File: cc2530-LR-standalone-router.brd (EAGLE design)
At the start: 44 x 24 mm, 16 parts, among them J1 629105150921, U1 AP2112K

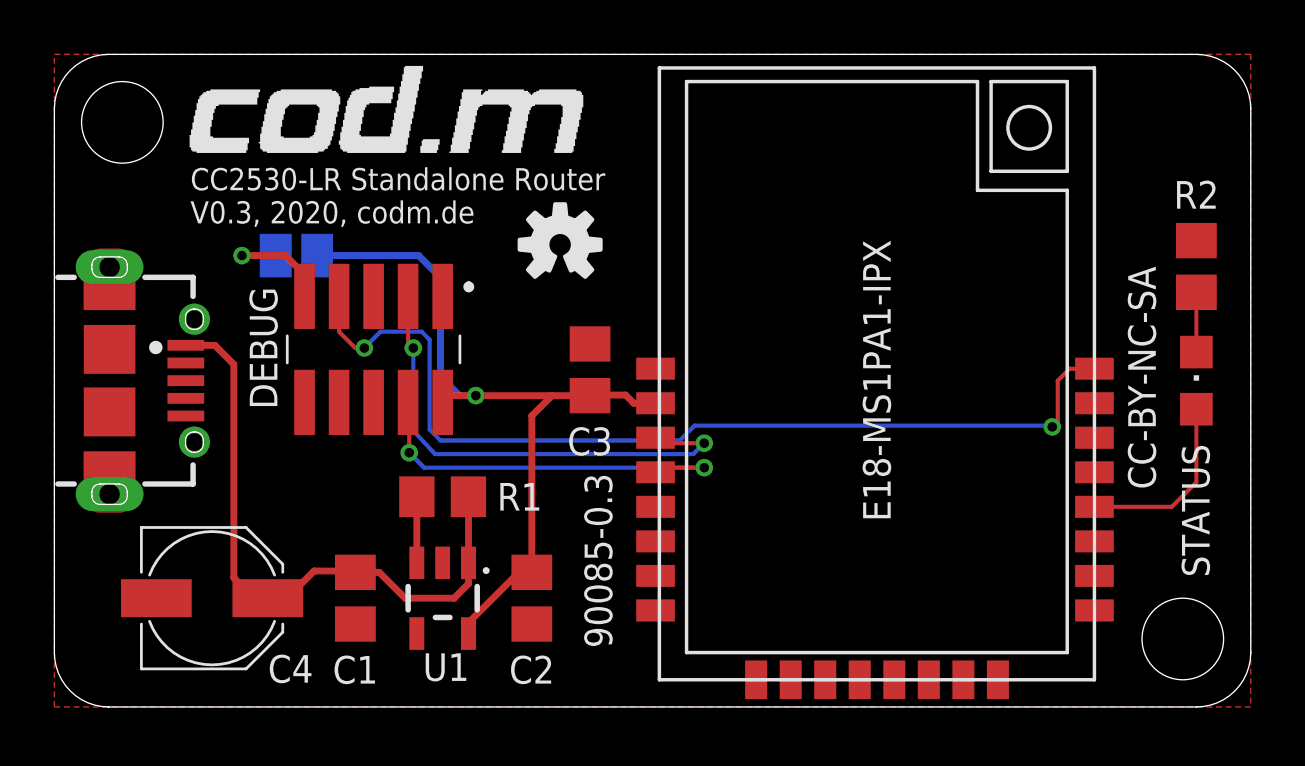
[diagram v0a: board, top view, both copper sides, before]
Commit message: minor rerouting
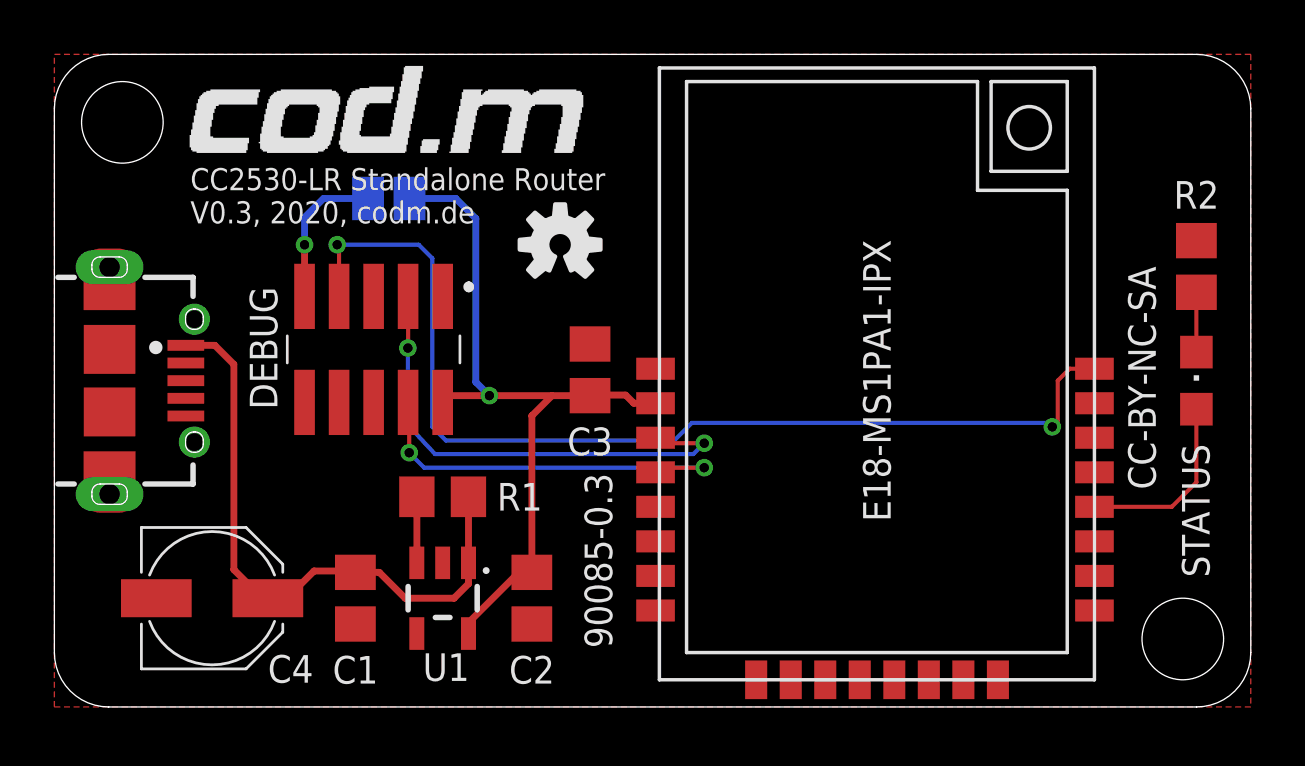
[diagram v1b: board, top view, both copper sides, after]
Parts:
- moved DBGVCC 4.00 mm to (12.3, 18.7)
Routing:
- net RST: track 35.2 -> 38.5 mm
- net VCC-DEBUG: track 4.63 -> 5.53 mm
- net VCC: track 28.5 -> 27.8 mm
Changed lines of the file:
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@@
 <attribute name="WORKING-VOLTAGE" value="30V(AC)" x="2.5" y="12" size="1.778" layer="27" rot="R270" display="off"/>
 </element>
-<element name="DBGVCC" library="jumper" library_urn="urn:adsk.eagle:library:252" package="SJ" package3d_urn="urn:adsk.eagle:package:15471/1" value="" x="8.9" y="16.6" smashed="yes" rot="MR0">
-<attribute name="NAME" x="12.151" y="17.843" size="1.27" layer="26" ratio="10" rot="MR0"/>
-<attribute name="POPULARITY" value="33" x="8.9" y="16.6" size="1.778" layer="28" rot="MR0" display="off"/>
-<attribute name="VALUE" x="8.4999" y="16.6" size="0.02" layer="28" rot="MR0"/>
+<element name="DBGVCC" library="jumper" library_urn="urn:adsk.eagle:library:252" package="SJ" package3d_urn="urn:adsk.eagle:package:15471/1" value="" x="12.3" y="18.7" smashed="yes" rot="MR0">
+<attribute name="NAME" x="15.551" y="19.943" size="1.27" layer="26" ratio="10" rot="MR0"/>
+<attribute name="POPULARITY" value="33" x="12.3" y="18.7" size="1.778" layer="28" rot="MR0" display="off"/>
+<attribute name="VALUE" x="11.8999" y="18.7" size="0.02" layer="28" rot="MR0"/>
 </element>
 <element name="U$2" library="codm" library_urn="urn:adsk.eagle:library:11602856" package="CODM-LOGO" package3d_urn="urn:adsk.eagle:package:11602917/4" value="" x="5" y="20.4" smashed="yes"/>
@@
 <wire x1="11.95" y1="4.95" x2="11.07" y2="4.95" width="0.254" layer="1"/>
 <wire x1="12.9" y1="4" x2="11.95" y2="4.95" width="0.254" layer="1"/>
-<wire x1="6.6" y1="12.6" x2="6.6" y2="4.75" width="0.254" layer="1"/>
-<wire x1="7.35" y1="4" x2="6.6" y2="4.75" width="0.254" layer="1"/>
+<wire x1="6.6" y1="12.6" x2="6.6" y2="5.05" width="0.254" layer="1"/>
 <wire x1="11.07" y1="4.95" x2="11.02" y2="5" width="0.254" layer="1"/>
 <wire x1="11.02" y1="5" x2="9.55" y2="5" width="0.254" layer="1"/>
@@
 <contactref element="C4" pad="+"/>
 <wire x1="7.85" y1="4" x2="8.55" y2="4" width="0.1524" layer="1"/>
-<wire x1="7.35" y1="4" x2="7.85" y2="4" width="0" layer="19" extent="1-1"/>
+<wire x1="6.6" y1="5.05" x2="7.65" y2="4" width="0.254" layer="1"/>
+<wire x1="7.65" y1="4" x2="7.85" y2="4" width="0.254" layer="1"/>
 </signal>
 <signal name="N$1">
@@
 <wire x1="17.0801" y1="4.95" x2="15.23" y2="3.0999" width="0.254" layer="1"/>
 <wire x1="17.0801" y1="4.95" x2="17.56" y2="4.95" width="0.254" layer="1"/>
-<wire x1="14.53" y1="11.45" x2="15.5" y2="11.45" width="0.254" layer="1"/>
+<wire x1="14.53" y1="11.45" x2="16" y2="11.45" width="0.254" layer="1"/>
 <wire x1="14.28" y1="11.2" x2="14.53" y2="11.45" width="0.254" layer="1"/>
 <wire x1="17.56" y1="4.95" x2="17.56" y2="10.71" width="0.254" layer="1"/>
 <contactref element="DBGVCC" pad="1"/>
-<wire x1="9.662" y1="16.6" x2="13.4" y2="16.6" width="0.254" layer="16"/>
-<wire x1="13.4" y1="16.6" x2="14.2" y2="15.8" width="0.254" layer="16"/>
-<wire x1="15.5" y1="11.45" x2="14.9" y2="11.45" width="0.254" layer="16"/>
-<wire x1="14.9" y1="11.45" x2="14.2" y2="12.15" width="0.254" layer="16"/>
-<wire x1="14.2" y1="15.8" x2="14.2" y2="12.15" width="0.254" layer="16"/>
-<via x="15.5" y="11.45" extent="1-16" drill="0.35" shape="octagon"/>
+<wire x1="14.762" y1="18.7" x2="15.5" y2="17.962" width="0.254" layer="16"/>
+<wire x1="14.762" y1="18.7" x2="13.062" y2="18.7" width="0.254" layer="16"/>
 <wire x1="19.7" y1="11.45" x2="19.72" y2="11.47" width="0.254" layer="1"/>
-<wire x1="22.11" y1="11.17" x2="22" y2="11.17" width="0.254" layer="1"/>
-<wire x1="22" y1="11.17" x2="21.31" y2="11.17" width="0.254" layer="1"/>
+<wire x1="22.11" y1="11.17" x2="21.31" y2="11.17" width="0.254" layer="1"/>
 <wire x1="21.31" y1="11.17" x2="21.01" y2="11.47" width="0.254" layer="1"/>
 <wire x1="21.01" y1="11.47" x2="19.72" y2="11.47" width="0.254" layer="1"/>
 <wire x1="17.56" y1="10.71" x2="18.3" y2="11.45" width="0.254" layer="1"/>
 <wire x1="18.3" y1="11.45" x2="19.7" y2="11.45" width="0.254" layer="1"/>
-<wire x1="15.5" y1="11.45" x2="18.3" y2="11.45" width="0.254" layer="1"/>
+<wire x1="16" y1="11.45" x2="18.3" y2="11.45" width="0.254" layer="1"/>
+<wire x1="15.5" y1="11.95" x2="16" y2="11.45" width="0.254" layer="16"/>
+<via x="16" y="11.45" extent="1-16" drill="0.35" shape="octagon"/>
+<wire x1="15.5" y1="17.962" x2="15.5" y2="11.95" width="0.254" layer="16"/>
 </signal>
 <signal name="DD">
@@
 <contactref element="U$5" pad="P2.2"/>
 <contactref element="DEBUG" pad="3"/>
-<wire x1="13.01" y1="15.1" x2="13.01" y2="13.39" width="0.1524" layer="1"/>
-<wire x1="13.01" y1="13.39" x2="13.2" y2="13.2" width="0.1524" layer="1"/>
-<via x="13.2" y="13.2" extent="1-16" drill="0.35" shape="octagon"/>
-<wire x1="13.2" y1="13.2" x2="13.2" y2="10.159884375" width="0.1524" layer="16"/>
-<wire x1="13.2" y1="10.159884375" x2="14" y2="9.3" width="0.1524" layer="16"/>
+<wire x1="13.01" y1="15.1" x2="13.01" y2="13.21" width="0.1524" layer="1"/>
+<wire x1="13.01" y1="13.21" x2="13" y2="13.2" width="0.1524" layer="1"/>
+<via x="13" y="13.2" extent="1-16" drill="0.35" shape="octagon"/>
+<wire x1="13" y1="13.2" x2="13" y2="10.37485625" width="0.1524" layer="16"/>
+<wire x1="13" y1="10.37485625" x2="14" y2="9.3" width="0.1524" layer="16"/>
 <wire x1="23.5" y1="9.3" x2="14" y2="9.3" width="0.1524" layer="16"/>
 <wire x1="23.5" y1="9.3" x2="23.9" y2="9.7" width="0.1524" layer="16"/>
@@
 <wire x1="36.9" y1="10.5" x2="36.7" y2="10.3" width="0.1524" layer="1"/>
 <via x="36.7" y="10.3" extent="1-16" drill="0.35" shape="octagon"/>
-<wire x1="36.7" y1="10.3" x2="36.6524" y2="10.3476" width="0.1524" layer="16"/>
-<wire x1="36.6524" y1="10.3476" x2="23.5476" y2="10.3476" width="0.1524" layer="16"/>
-<wire x1="23.5476" y1="10.3476" x2="23" y2="9.8" width="0.1524" layer="16"/>
-<wire x1="23" y1="9.8" x2="14.2" y2="9.8" width="0.1524" layer="16"/>
-<via x="11.4" y="13.2" extent="1-16" drill="0.35" shape="octagon"/>
-<wire x1="13.8012" y1="13.50760625" x2="13.50760625" y2="13.8012" width="0.1524" layer="16"/>
-<wire x1="13.50760625" y1="13.8012" x2="11.99239375" y2="13.8012" width="0.1524" layer="16"/>
-<wire x1="13.8012" y1="10.1988" x2="13.8012" y2="13.50760625" width="0.1524" layer="16"/>
-<wire x1="11.99239375" y1="13.8012" x2="11.4" y2="13.20880625" width="0.1524" layer="16"/>
-<wire x1="11.4" y1="13.20880625" x2="11.4" y2="13.2" width="0.1524" layer="16"/>
-<wire x1="11.4" y1="13.2" x2="11.07" y2="13.2" width="0.1524" layer="1"/>
-<wire x1="11.07" y1="13.2" x2="10.47" y2="13.8" width="0.1524" layer="1"/>
-<wire x1="10.47" y1="13.8" x2="10.47" y2="15.1" width="0.1524" layer="1"/>
-<wire x1="14.2" y1="9.8" x2="13.8012" y2="10.1988" width="0.1524" layer="16"/>
+<wire x1="36.7" y1="10.3" x2="36.5524" y2="10.4476" width="0.1524" layer="16"/>
+<wire x1="36.5524" y1="10.4476" x2="23.4476" y2="10.4476" width="0.1524" layer="16"/>
+<wire x1="23.4476" y1="10.4476" x2="22.8" y2="9.8" width="0.1524" layer="16"/>
 <wire x1="36.9" y1="12" x2="37.34" y2="12.44" width="0.1524" layer="1"/>
 <wire x1="37.34" y1="12.44" x2="38.25" y2="12.44" width="0.1524" layer="1"/>
+<wire x1="14.4" y1="9.8" x2="13.9" y2="10.3" width="0.1524" layer="16"/>
+<wire x1="22.8" y1="9.8" x2="14.4" y2="9.8" width="0.1524" layer="16"/>
+<wire x1="13.4" y1="17" x2="10.4" y2="17" width="0.1524" layer="16"/>
+<via x="10.4" y="17" extent="1-16" drill="0.35" shape="octagon"/>
+<wire x1="10.4" y1="17" x2="10.47" y2="16.93" width="0.1524" layer="1"/>
+<wire x1="10.47" y1="16.93" x2="10.47" y2="15.1" width="0.1524" layer="1"/>
+<wire x1="13.9" y1="10.3" x2="13.9" y2="16.5" width="0.1524" layer="16"/>
+<wire x1="13.9" y1="16.5" x2="13.4" y2="17" width="0.1524" layer="16"/>
 </signal>
 <signal name="VCC-DEBUG">
 <contactref element="DBGVCC" pad="2"/>
 <contactref element="DEBUG" pad="9"/>
-<wire x1="8.138" y1="16.6" x2="6.9" y2="16.6" width="0.254" layer="16"/>
-<via x="6.9" y="16.6" extent="1-16" drill="0.35" shape="octagon"/>
-<wire x1="6.9" y1="16.6" x2="8.5" y2="16.6" width="0.254" layer="1"/>
-<wire x1="9.2" y1="15.9" x2="9.2" y2="15.1" width="0.254" layer="1"/>
-<wire x1="9.2" y1="15.9" x2="8.5" y2="16.6" width="0.254" layer="1"/>
+<wire x1="11.538" y1="18.7" x2="9.9" y2="18.7" width="0.254" layer="16"/>
+<wire x1="9.9" y1="18.7" x2="9.2" y2="18" width="0.254" layer="16"/>
+<wire x1="9.2" y1="18" x2="9.2" y2="17" width="0.254" layer="16"/>
+<via x="9.2" y="17" extent="1-16" drill="0.35" shape="octagon"/>
+<wire x1="9.2" y1="17" x2="9.2" y2="15.1" width="0.254" layer="1"/>
 </signal>
 <signal name="N$3">
